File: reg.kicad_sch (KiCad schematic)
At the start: 20 parts, among them Q5 NJVMJD45H11T4G, Q6 PNP, U2 AD817

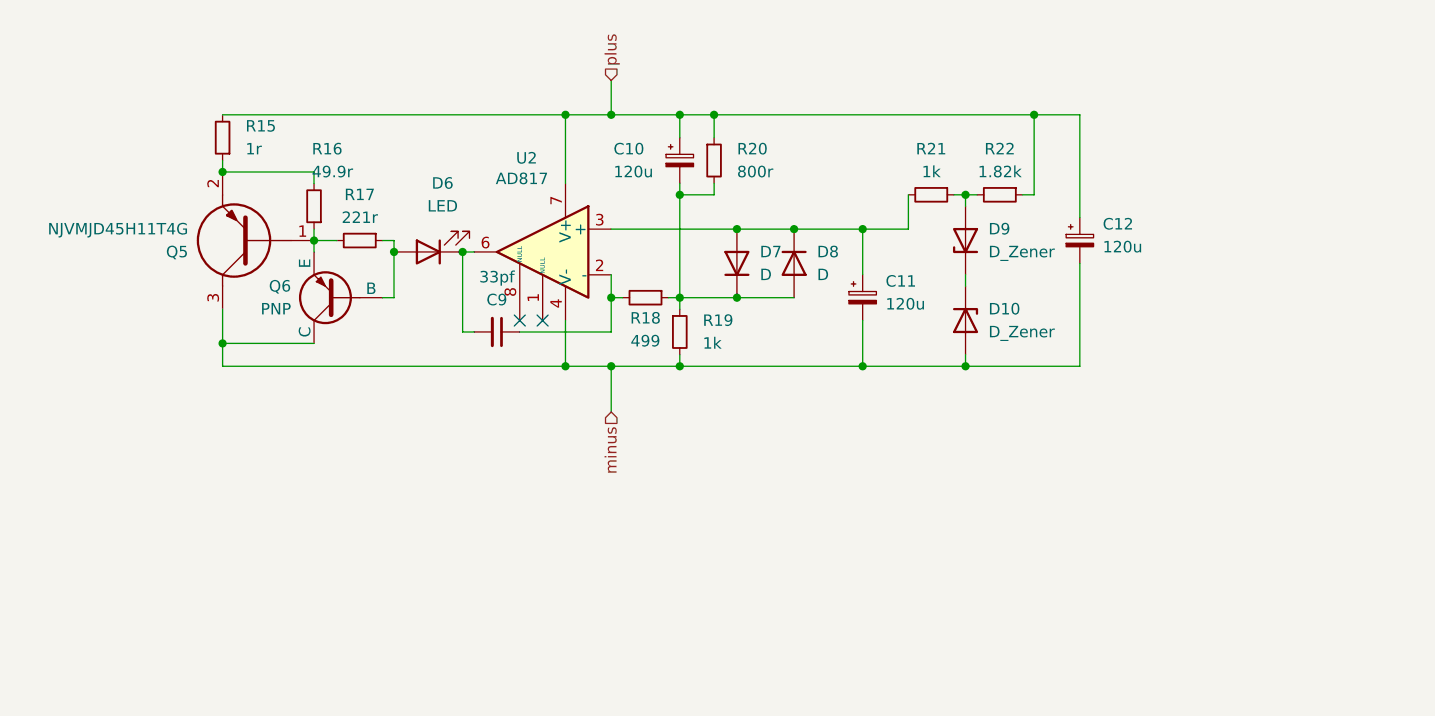
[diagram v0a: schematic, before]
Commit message: Current design with SMD MOSFET (before switching to THT)
🤖 Generated with [Claude Code](https://claude.ai/code)

Co-Authored-By: Claude <noreply@anthropic.com>
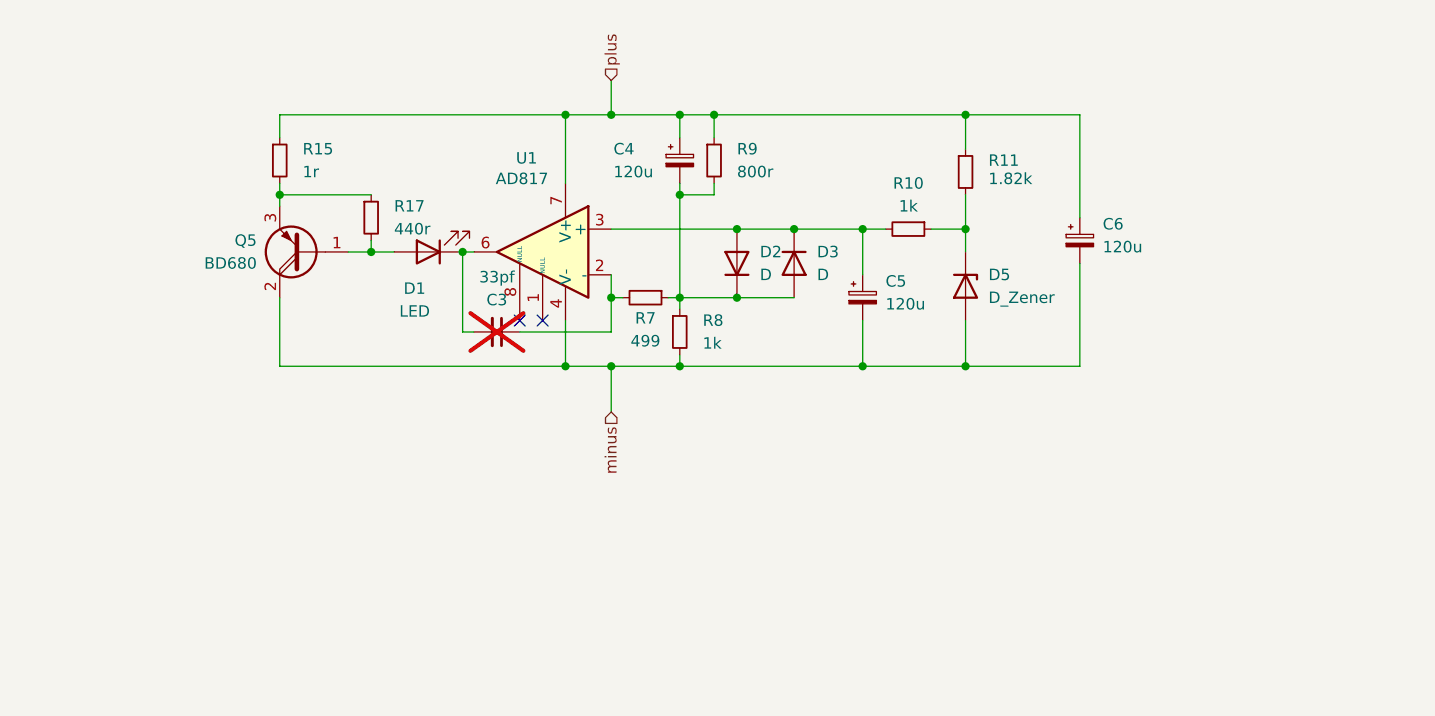
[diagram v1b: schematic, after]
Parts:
- removed D9: D_Zener, Diode_SMD:D_MiniMELF, symbol Device:D_Zener
- removed Q5: NJVMJD45H11T4G, Samacsys:DPAK_(SINGLE-GAUGE)_TO-252(369C)_ISSUE_F, symbol Samacsys:NJVMJD45H11T4G
- removed Q6: PNP, Package_TO_SOT_SMD:SOT-23-3, symbol Simulation_SPICE:PNP
- removed R16: 49.9r, Resistor_SMD:R_1206_3216Metric, symbol Device:R_Small
- added Q5: BD680, Package_TO_SOT_THT:TO-126-3_Vertical, symbol Transistor_BJT:Q_PNP_Darlington_BCE
- C3: renamed from C9; now not fitted
- D2: renamed from D7; footprint Diode_SMD:D_SOD-123F -> Diode_SMD:D_0805_2012Metric
- D3: renamed from D8; footprint Diode_SMD:D_SOD-123F -> Diode_SMD:D_0805_2012Metric
- D5: renamed from D10; footprint Diode_SMD:D_MiniMELF -> Diode_SMD:D_0805_2012Metric
- R10: renamed from R21; footprint Resistor_SMD:R_1206_3216Metric -> Resistor_SMD:R_0805_2012Metric
- R11: renamed from R22; footprint Resistor_SMD:R_1206_3216Metric -> Resistor_SMD:R_0805_2012Metric
- R15: footprint Resistor_SMD:R_1206_3216Metric -> Resistor_SMD:R_0805_2012Metric
- R17: value 221r -> 440r; footprint Resistor_SMD:R_1206_3216Metric -> Resistor_SMD:R_0805_2012Metric
- R7: renamed from R18; footprint Resistor_SMD:R_1206_3216Metric -> Resistor_SMD:R_0805_2012Metric
- R8: renamed from R19; footprint Resistor_SMD:R_MELF_MMB-0207 -> Resistor_SMD:R_0805_2012Metric
- R9: renamed from R20; footprint Resistor_SMD:R_MELF_MMB-0207 -> Resistor_SMD:R_0805_2012Metric
- renumbered C10 to C4, C11 to C5, C12 to C6, D6 to D1, U2 to U1
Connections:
- net minus: now also Q5.2 (C)
- net plus: now also R15.1; no longer R15.2
- net at D5.1 (K): now also R10.1, R11.2
- net at R17.2: now also D1.2 (A), Q5.1 (B)
- net at R17.1: now also R15.2, Q5.3 (E); no longer D1.2 (A)
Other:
- moved on the sheet: D5, R10, R11

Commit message: Single rail design - initial branch
🤖 Generated with [Claude Code](https://claude.ai/code)

Co-Authored-By: Claude <noreply@anthropic.com>
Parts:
- added D29, D30, D31: gled, symbol Device:LED_Small
- added D33: rled, symbol Device:LED_Small
- added D4: gled, symbol Device:LED
- added Q7: PNP, symbol Simulation_SPICE:PNP
- added R24: 150r, Resistor_SMD:R_0805_2012Metric, symbol Device:R_Small
- R9: value 800r -> 1k
- U1: symbol Amplifier_Operational:AD817 -> Simulation_SPICE:OPAMP
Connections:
- net at C3.2, D1.1 (K): now also U1.5; no longer U1.6
- net at C5.1, D2.2 (A), D3.1 (K)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: now also U1.1 (+); no longer U1.3 (+)
- net minus renamed -
- net plus renamed +
- net +: now also U1.3 (V+); no longer U1.7 (V+)
- new net: D31.1 (K), D33.2 (A)
- new net: D30.1 (K), D31.2 (A)
- new net: D4.1 (K), Q7.1 (C)
- new net: D4.2 (A), Q7.2 (B), R24.2
- new net: Q7.3 (E), R24.1
- new net: D29.1 (K), D30.2 (A)
- no-connect marks 2 -> 0
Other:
- moved on the sheet: C4, D2, D5, R11, R8, R9

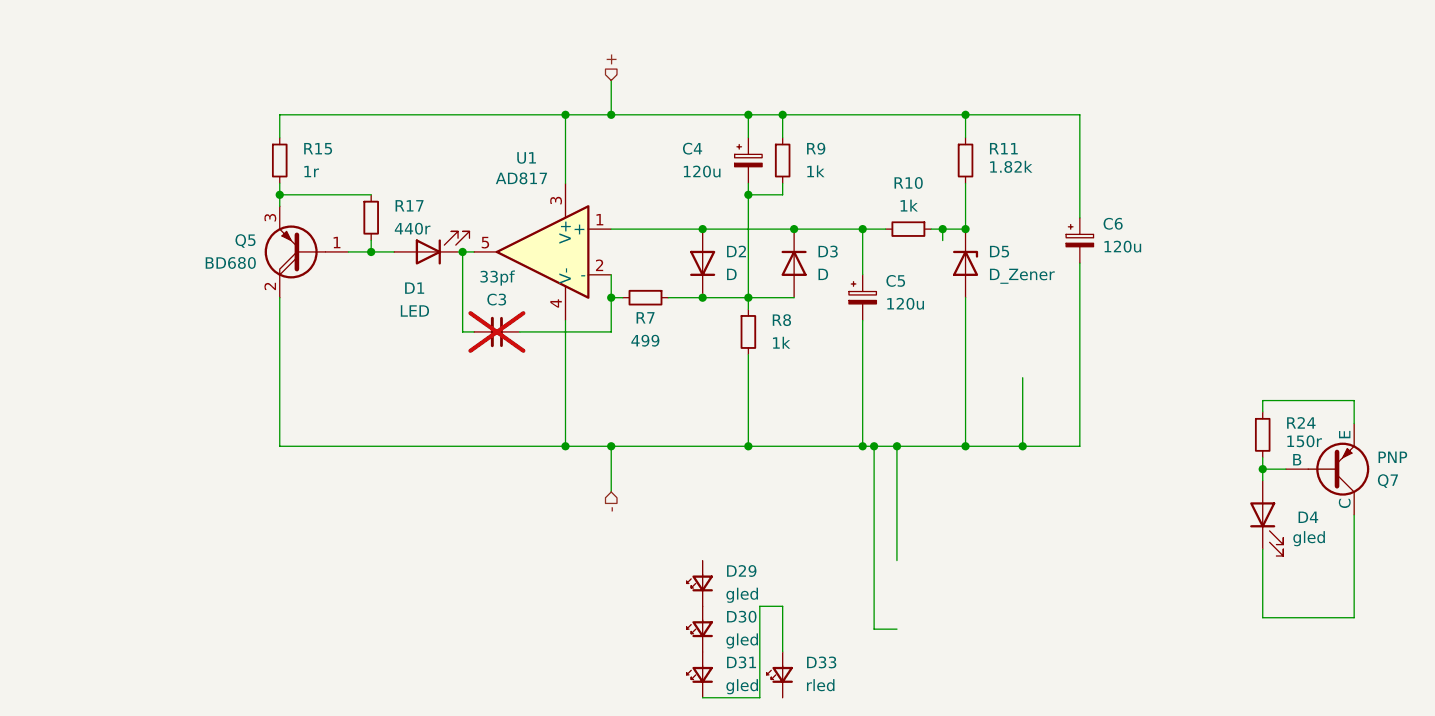
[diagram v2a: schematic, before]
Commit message: Working KiCad design - simulates and looks good
Re-read Walt's manual and realized we needed a fattier current source as he recommended a much larger voltage drop than we had assumed. Added GLED VREF. We get a 90mA current.

🤖 Generated with [Claude Code](https://claude.ai/code)

Co-Authored-By: Claude <noreply@anthropic.com>
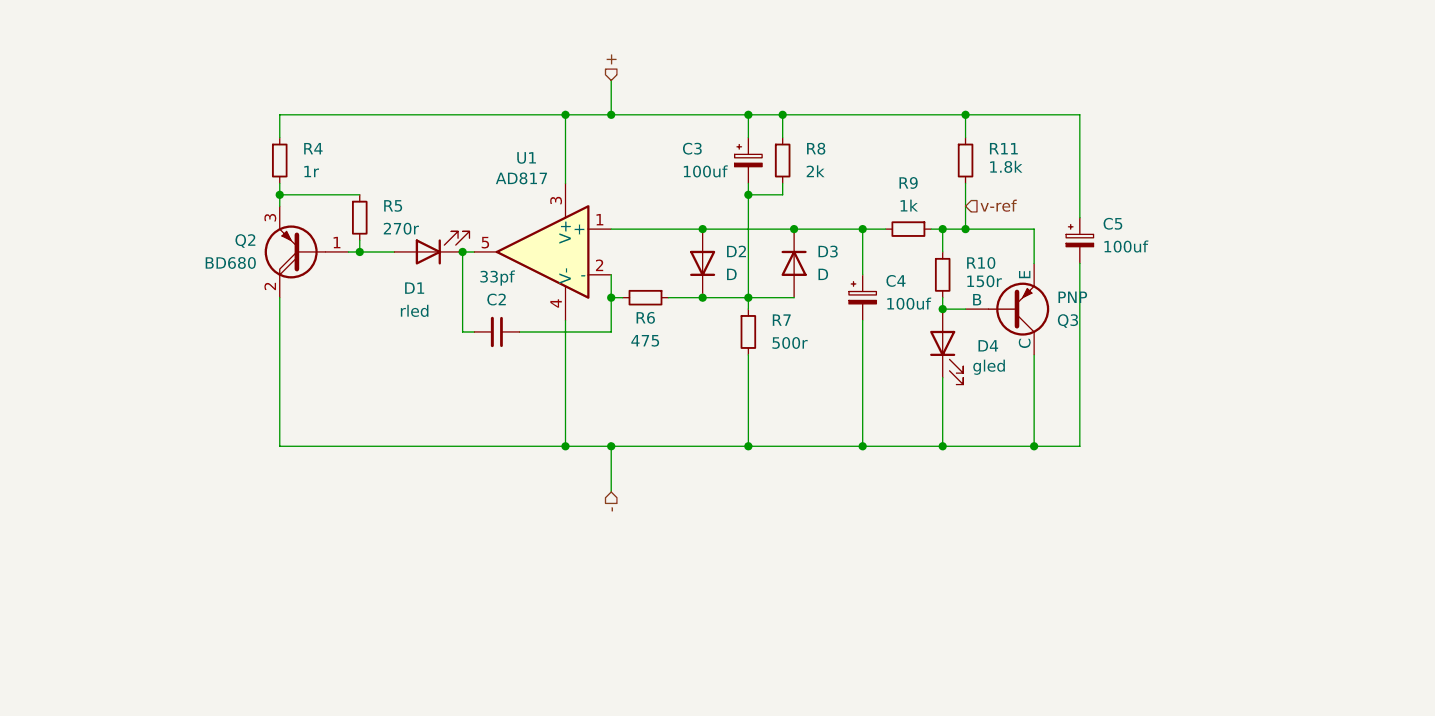
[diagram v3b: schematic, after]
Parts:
- removed D29, D30, D31: gled, symbol Device:LED_Small
- removed D33: rled, symbol Device:LED_Small
- removed D5: D_Zener, Diode_SMD:D_0805_2012Metric, symbol Device:D_Zener
- C2: renamed from C3; now fitted
- C3: renamed from C4; value 120u -> 100uf
- C4: renamed from C5; value 120u -> 100uf
- C5: renamed from C6; value 120u -> 100uf
- D1: value LED -> rled
- R11: value 1.82k -> 1.8k
- R5: renamed from R17; value 440r -> 270r
- R6: renamed from R7; value 499 -> 475
- R7: renamed from R8; value 1k -> 500r
- R8: renamed from R9; value 1k -> 2k
- renumbered Q5 to Q2, Q7 to Q3, R24 to R10, R15 to R4, R10 to R9
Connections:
- net -: now also D4.1 (K), Q3.1 (C)
- net v-ref: now reaches R11.2, R9.1
- net v-ref: now also Q3.3 (E), R10.1
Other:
- moved on the sheet: Q3, R10, R5

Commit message: Half layout done
🤖 Generated with [Claude Code](https://claude.ai/code)

Co-Authored-By: Claude <noreply@anthropic.com>
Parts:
- removed Q2: BD680, Package_TO_SOT_THT:TO-126-3_Vertical, symbol Transistor_BJT:Q_PNP_Darlington_BCE
- removed Q3: PNP, symbol Simulation_SPICE:PNP
- added Q2: D45H11G, Package_TO_SOT_THT:TO-220-3_Vertical, symbol Transistor_BJT:Q_PNP_BCE
- added Q3: MMBT2907AL, Package_TO_SOT_SMD:SOT-23-3, symbol Transistor_BJT:Q_PNP_BEC
- added Q4: ZTX951, Package_TO_SOT_THT:TO-92Flat, symbol Transistor_BJT:Q_PNP_CBE
- added R7: 50r, Resistor_SMD:R_0805_2012Metric, symbol Device:R_Small
- D4: footprint (none) -> LED_SMD:LED_0805_2012Metric
- R8: renamed from R5; value 270r -> 221r
- renumbered C2 to C3, C3 to C4, C4 to C5, C5 to C6, R7 to R10, R8 to R11, R9 to R12, R10 to R13, R11 to R14, R4 to R6, R6 to R9
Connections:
- net -: now also Q2.2 (C), Q3.3 (C), Q4.1 (C)
- net v-ref: now also Q4.3 (E)
- net at D4.2 (A), R13.2: now also Q4.2 (B)
- net at R8.1: now also Q2.1 (B), Q3.2 (E), R7.2; no longer R6.2
- net at D1.2 (A), R8.2: now also Q3.1 (B)
- new net: Q2.3 (E), R6.2, R7.1
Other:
- moved on the sheet: R6, R8
